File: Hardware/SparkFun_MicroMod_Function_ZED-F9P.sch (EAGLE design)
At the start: 107 parts, among them J10 QWIIC_RA, J11 Bus Selection, J12 USB Female Type C Connector, J2 MICROMOD_STANDARD, J3 QWIIC_RA, J4 U.FL, J5 455-1750-1-ND, J8 Bus Selection, Q1 DMP21D0UT, U1 EEPROM, U10 OPA344, U11 74LVC4066D_QUAD_BILATERAL_SWI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, U12 74LVC4066D_QUAD_BILATERAL_SWI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, U2 U-BLOX_ZED-F9P, U3 FIN1017MXSOIC-8, U4 SN74AUP1T04DCK, U5 SN74LVC1G66DRYR, U6 74LVC541ABQ, U7 3.3V, U9 SN74AUP1T04DCK

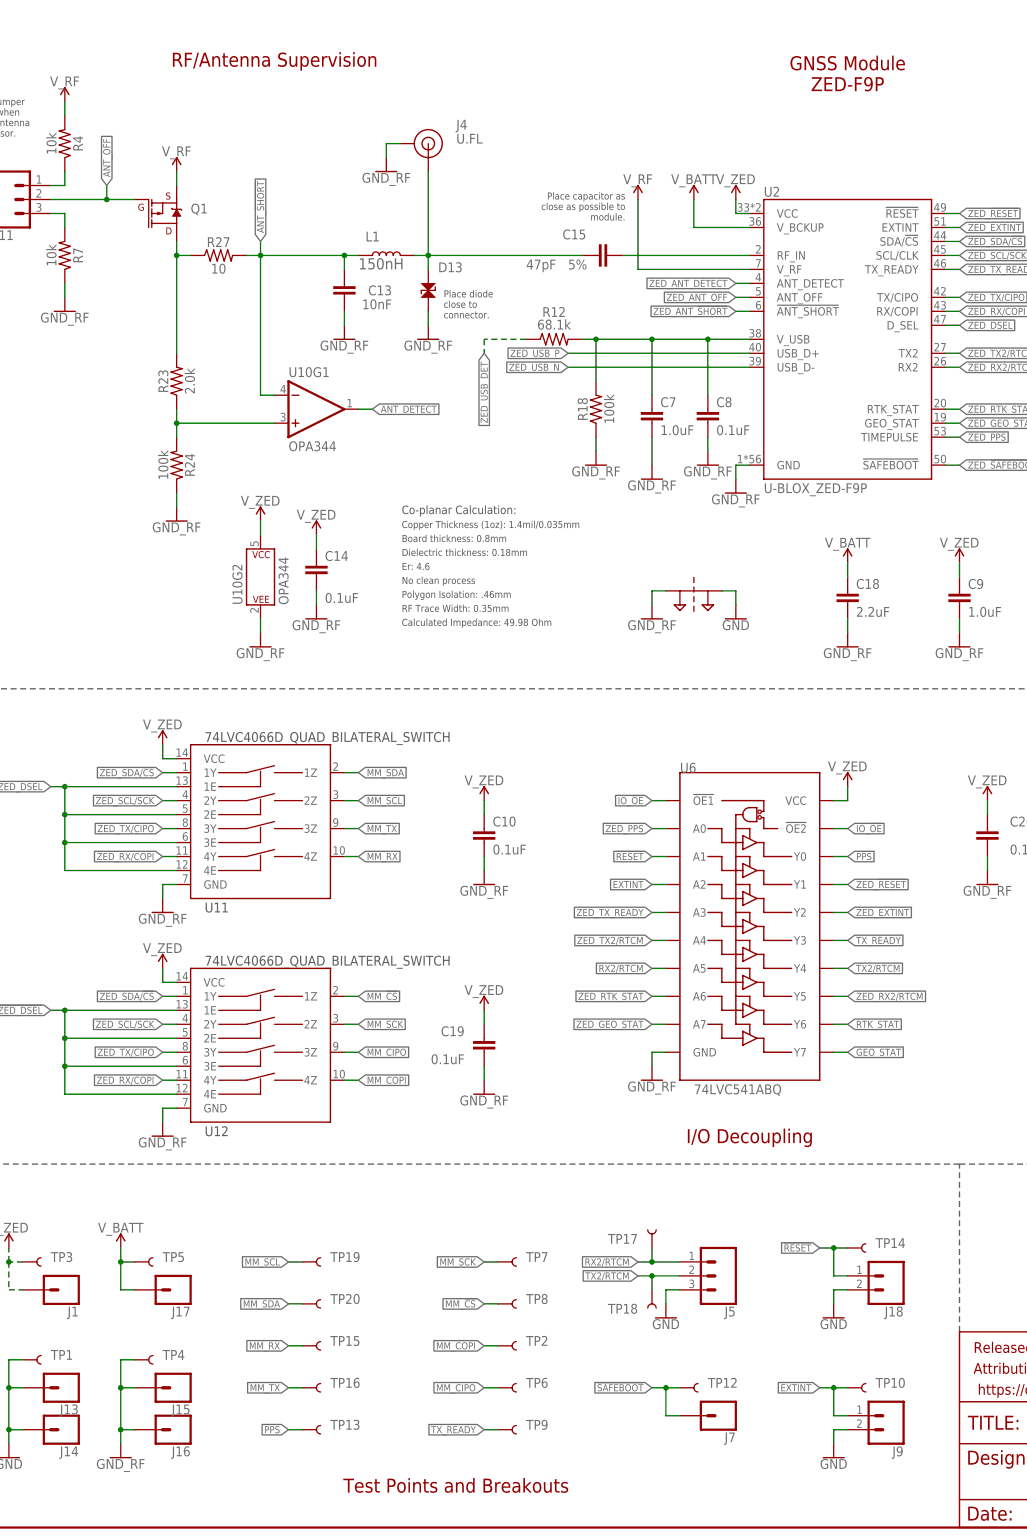
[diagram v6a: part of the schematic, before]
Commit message: ERC run and fixes applied.
Forgot to do that before previous commit.
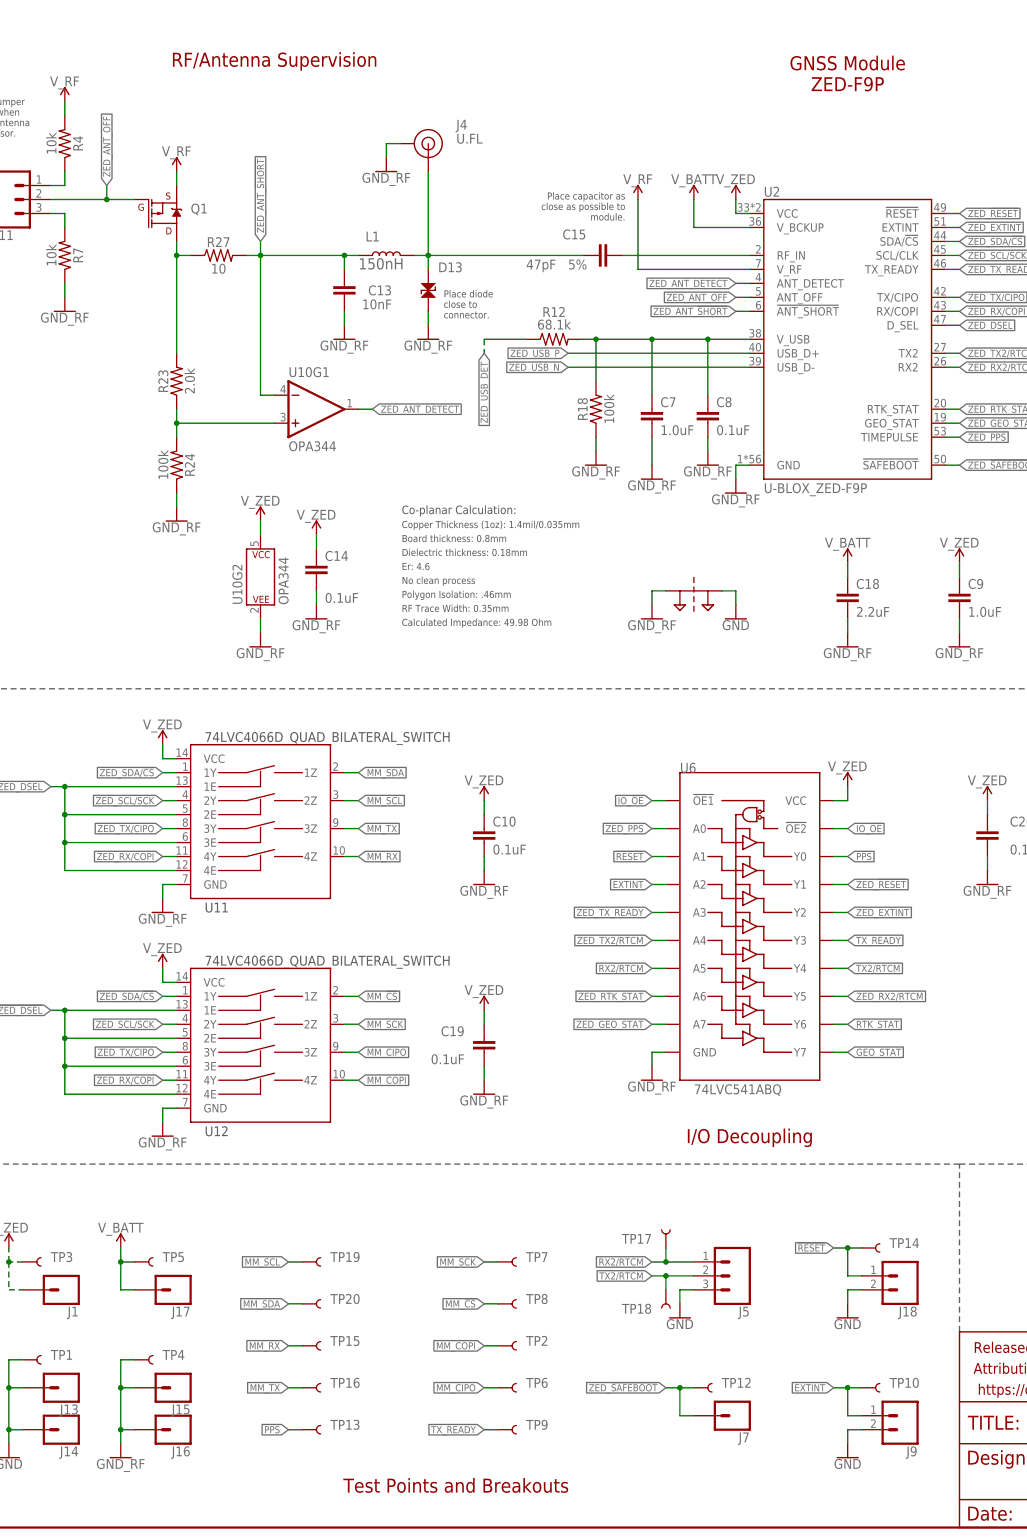
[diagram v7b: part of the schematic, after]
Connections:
- removed net !SAFEBOOT!: J7.1, TP12.1
- removed net ANT_!SHORT!: C13.1, L1.1, R27.2, U10G1.-IN
- removed net ANT_DETECT: U10G1.OUT
- removed net ANT_OFF: J11.2, Q1.G
- new net N$14: C7.1, C8.1, R12.2, R18.2, U2.V_USB
- net ZED_!SAFEBOOT!: now also J7.1, TP12.1
- net ZED_ANT_!SHORT!: now also C13.1, L1.1, R27.2, U10G1.-IN
- net ZED_ANT_DETECT: now also U10G1.OUT
- net ZED_ANT_OFF: now also J11.2, Q1.G
- net ZED_USB_DET: no longer C7.1, C8.1, R12.2, R18.2, U2.V_USB
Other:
- moved on the sheet: J18, J5, J7, J9, TP10, TP12, TP14, TP17, TP18

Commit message: First day of layout.
Laid out most of the board with airwires. Have a rough idea of grounding so far so good. Have had to replace a fair bit of components for smaller ones. Those 0603's look massive on such a small board.
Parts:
- removed C17, C19, C20: 0.1uF, SparkFun-Capacitors:0.1UF-0603-25V-(+80/-20%)
- removed C18: 2.2uF, SparkFun-Capacitors:2.2UF-0402_TIGHT-10V-10%-X5R
- removed D13: PESD0402, SparkFun-DiscreteSemi:PESD0402
- removed D9: 3A/10V/280mV, SparkFun-DiscreteSemi:DIODE-SCHOTTKY-BAT60A
- removed JP9: JUMPER-SMT_2_NC_TRACE_SILK, SparkFun-Jumpers:JUMPER-SMT_2_NC_TRACE_SILK
- removed R20: 1k, SparkFun-Resistors:1KOHM-0603-1/10W-1%
- removed R23: 2.0k, SparkFun-Resistors:2.0KOHM-0603-1/10W-5%
- removed TP20: TEST-POINT3, SparkFun-Connectors:TEST-POINT3
- removed U12: 74LVC4066D_QUAD_BILATERAL_SWITCH, SparkFun-IC-Logic:74LVC4066D_QUAD_BILATERAL_SWITCH
- added C16, C4, C6: 0.1uF, SparkFun-Capacitors:0.1UF-0402T-16V-10%
- added C5: 10nF, SparkFun-Capacitors:10NF-0402T-25V-10%-X7R-WE
- added D2: 3A/10V/280mV, SparkFun-DiscreteSemi:DIODE-SCHOTTKY-BAT60A
- added D8: PESD0402-0402T, SparkFun-DiscreteSemi:PESD0402-0402T
- added JP6: JUMPER-SMT_2_NC_TRACE_SILK, SparkFun-Jumpers:JUMPER-SMT_2_NC_TRACE_SILK
- added R15: 68.1k, SparkFun-Resistors:68.1KOHM-0603-1/10W-1%
- added R17: 10k, SparkFun-Resistors:10KOHM-0603-1/10W-1%
- added TP11: TEST-POINT3, SparkFun-Connectors:TEST-POINT3
- added U8: U-BLOX_ZED-F9P, MicroMod_Function_GNSS_ublox_ZED_F9P:U-BLOX_ZED-F9P
- C1, C3, C9: device SparkFun-Capacitors:1.0UF-0603-16V-10% -> SparkFun-Capacitors:1.0UF-0402T-16V-10%
- C10, C14: device SparkFun-Capacitors:0.1UF-0402-16V-10% -> SparkFun-Capacitors:0.1UF-0402T-16V-10%
- C11: value 0.1uF -> 2.2uF; device SparkFun-Capacitors:0.1UF-0603-25V-(+80/-20%) -> SparkFun-Capacitors:2.2UF-0402_TIGHT-10V-10%-X5R
- C12: value 0.1uF -> 1.0uF; device SparkFun-Capacitors:0.1UF-0402-16V-10% -> SparkFun-Capacitors:1.0UF-0402T-16V-10%
- C13: value 10nF -> 0.1uF; device SparkFun-Capacitors:10NF-0402T-25V-10%-X7R-WE -> SparkFun-Capacitors:0.1UF-0402T-16V-10%
- C15: value CBR04C470J5GAC -> 0.1uF; device MicroMod_Function_GNSS_ublox_ZED_F9P:CBR04C470J5GAC -> SparkFun-Capacitors:0.1UF-0402T-16V-10%
- C2: device SparkFun-Capacitors:0.1UF-0603-25V-(+80/-20%) -> SparkFun-Capacitors:0.1UF-0402T-16V-10%
- C7: value 1.0uF -> 0.1uF; device SparkFun-Capacitors:1.0UF-0603-16V-10% -> SparkFun-Capacitors:0.1UF-0402T-16V-10%
- C8: value 0.1uF -> CBR04C470J5GAC; device SparkFun-Capacitors:0.1UF-0402T-16V-10% -> MicroMod_Function_GNSS_ublox_ZED_F9P:CBR04C470J5GAC
- D3: value BLUE -> PRTR5V0U2F; device SparkFun-LED:LED-BLUE0603 -> SparkFun-IC-Power:PRTR5V0U2F
- D4: value BLUE -> 0.5A/40V/420mV; device SparkFun-LED:LED-BLUE0603 -> SparkFun-DiscreteSemi:DIODE-SCHOTTKY-PMEG4005EJ
- D6: value PRTR5V0U2F -> BLUE; device SparkFun-IC-Power:PRTR5V0U2F -> SparkFun-LED:LED-BLUE0603
- D7: value 0.5A/40V/420mV -> BLUE; device SparkFun-DiscreteSemi:DIODE-SCHOTTKY-PMEG4005EJ -> SparkFun-LED:LED-BLUE0603
- J1: value (none) -> USB Female Type C Connector; device SparkFun-Connectors:CONN_01 -> SparkFun-Connectors:USB_C_4-LAYER-ISOLATED
- J10: value QWIIC_RA -> U.FL; device SparkFun-Connectors:QWIIC_CONNECTORJS-1MM -> SparkFun-Connectors:U.FL2PIN
- J11: value Bus Selection -> 455-1750-1-ND; device SparkFun-Connectors:CONN_03LOCK -> SparkFun-Connectors:CONN_03
- J12: value USB Female Type C Connector -> (none); device SparkFun-Connectors:USB_C_4-LAYER-ISOLATED -> SparkFun-Connectors:CONN_01
- J13, J14: device SparkFun-Connectors:CONN_01 -> SparkFun-Connectors:CONN_02
- J15, J16: value (none) -> QWIIC_RA; device SparkFun-Connectors:CONN_01 -> SparkFun-Connectors:QWIIC_CONNECTORJS-1MM
- J17: device SparkFun-Connectors:CONN_01 -> SparkFun-Connectors:CONN_04PTH
- J18: value (none) -> Bus Selection; device SparkFun-Connectors:CONN_02 -> SparkFun-Connectors:CONN_03LOCK
- J3: value QWIIC_RA -> Bus Selection; device SparkFun-Connectors:QWIIC_CONNECTORJS-1MM -> SparkFun-Connectors:CONN_03LOCK
- J4: value U.FL -> (none); device SparkFun-Connectors:U.FL2PIN -> SparkFun-Connectors:CONN_01
- J5: value 455-1750-1-ND -> (none); device SparkFun-Connectors:CONN_03 -> SparkFun-Connectors:CONN_01
- J6: device SparkFun-Connectors:CONN_04PTH -> SparkFun-Connectors:CONN_01
- J8: value Bus Selection -> (none); device SparkFun-Connectors:CONN_03LOCK -> SparkFun-Connectors:CONN_01
- J9: device SparkFun-Connectors:CONN_02 -> SparkFun-Connectors:CONN_01
- R10: value 27 -> 10k; device SparkFun-Resistors:27OHM -> SparkFun-Resistors:10KOHM-0603-1/10W-1%
- R11: value 3.3k -> 10k; device SparkFun-Resistors:3.3KOHM-0603-1/10W-1% -> SparkFun-Resistors:10KOHM-0603-1/10W-1%
- R12: value 68.1k -> 1k; device SparkFun-Resistors:68.1KOHM-0603-1/10W-1% -> SparkFun-Resistors:1KOHM-0603-1/10W-1%; RESISTANCE (none) -> 1k
- R3: value 10k -> 5.1k; device SparkFun-Resistors:10KOHM-0603-1/10W-1% -> SparkFun-Resistors:5.1KOHM5.1KOHM-0603-1/10W-1%
- R4: value 10k -> 3.3k; device SparkFun-Resistors:10KOHM-0603-1/10W-1% -> SparkFun-Resistors:3.3KOHM-0603-1/10W-1%
- R5, R6: value 1k -> 27; device SparkFun-Resistors:1KOHM-0603-1/10W-1% -> SparkFun-Resistors:27OHM
- R7: value 10k -> 1k; device SparkFun-Resistors:10KOHM-0603-1/10W-1% -> SparkFun-Resistors:1KOHM-0603-1/10W-1%
- R8: value 5.1k -> 1k; device SparkFun-Resistors:5.1KOHM5.1KOHM-0603-1/10W-1% -> SparkFun-Resistors:1KOHM-0603-1/10W-1%
- R9: value 27 -> 1k; device SparkFun-Resistors:27OHM -> SparkFun-Resistors:1KOHM-0603-1/10W-1%
- U1: value EEPROM -> SN74LVC1G66DRYR; device SparkFun-IC-Memory:EEPROM-I2C512K -> MicroMod_Function_GNSS_ublox_ZED_F9P:SN74LVC1G66DRYR
- U10: value OPA344 -> SN74AUP1T04DCK; device SparkFun-IC-Amplifiers:OPA344 -> MicroMod_Function_GNSS_ublox_ZED_F9P:SN74AUP1T04DCK
- U11: value 74LVC4066D_QUAD_BILATERAL_SWITCH -> SN74AUP1T04DCK; device SparkFun-IC-Logic:74LVC4066D_QUAD_BILATERAL_SWITCH -> MicroMod_Function_GNSS_ublox_ZED_F9P:SN74AUP1T04DCK
- U2: value U-BLOX_ZED-F9P -> 3.3V; device MicroMod_Function_GNSS_ublox_ZED_F9P:U-BLOX_ZED-F9P -> SparkFun-IC-Power:V_REG_AP2112K-3.3V
- U3: value FIN1017MXSOIC-8 -> EEPROM; device MicroMod_Function_GNSS_ublox_ZED_F9P:FIN1017MXSOIC-8 -> SparkFun-IC-Memory:EEPROM-I2C512K
- U4: value SN74AUP1T04DCK -> 74LVC4066D_QUAD_BILATERAL_SWITCH; device MicroMod_Function_GNSS_ublox_ZED_F9P:SN74AUP1T04DCK -> SparkFun-IC-Logic:74LVC4066D_QUAD_BILATERAL_SWITCH
- U5: value SN74LVC1G66DRYR -> 74LVC4066D_QUAD_BILATERAL_SWITCH; device MicroMod_Function_GNSS_ublox_ZED_F9P:SN74LVC1G66DRYR -> SparkFun-IC-Logic:74LVC4066D_QUAD_BILATERAL_SWITCH
- U6: value 74LVC541ABQ -> OPA344; device MicroMod_Function_GNSS_ublox_ZED_F9P:74LVC541ABQ -> SparkFun-IC-Amplifiers:OPA344
- U7: value 3.3V -> 74LVC541ABQ; device SparkFun-IC-Power:V_REG_AP2112K-3.3V -> MicroMod_Function_GNSS_ublox_ZED_F9P:74LVC541ABQ
- U9: value SN74AUP1T04DCK -> FIN1017MXSOIC-8; device MicroMod_Function_GNSS_ublox_ZED_F9P:SN74AUP1T04DCK -> MicroMod_Function_GNSS_ublox_ZED_F9P:FIN1017MXSOIC-8
- renumbered D11 to D5, JP13 to JP3, R18 to R16, R24 to R13, R27 to R14, SUPPLY35 to SUPPLYTIE1
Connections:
- removed net VDD: C1.1, J1.1, R3.2, TP3.1, U7.OUT
- net !RESET!: now also J13.1, TP18.1, U7.A1; no longer J18.1, TP14.1, U6.A1
- net !ZED_DSEL!: now also U11.Y, U5.1E, U5.2E, U5.3E, U5.4E; no longer U12.1E, U12.2E, U12.3E, U12.4E, U9.Y
- net 3.3V: now also C14.1, D4.A, J15.2, J16.2, U9.VCC; no longer C12.1, D7.A, J10.2, J3.2, U1.VCC
- net 5V: now also C1.1, D2.C, U2.IN; no longer C3.1, D9.C, U5.CTRL_IN, U5.VCC, U7.IN
- net A0: now also U3.A0; no longer U1.A0
- net A1: now also U3.A1; no longer U1.A1
- net A2: now also U3.A2; no longer U1.A2
- net EWP: now also JP2.2, U3.WP; no longer JP1.2, U1.WP
- net EXTINT: now also J14.1, TP19.1, U7.A2; no longer J9.1, TP10.1, U6.A2
- net GEO_STAT: now also U7.Y7; no longer U6.Y7
- net GND: now also C14.2, D3.2, J1.GND, J11.3, J13.2, J14.2, J15.1, J16.1, J17.1, J17.4, J5.1, JP2.1, JP4.2, JP6.1, R3.1, TP2.1, U1.VSS, U2.GND, U9.GND; no longer C12.2, D6.2, J10.1, J12.GND, J13.1, J14.1, J18.2, J3.1, J5.3, J6.4, J9.2, JP1.1, JP4.1, JP9.2, R8.1, TP1.1, U1.GND, U5.VSS, U7.GND
- net GND_RF: now also C11.2, C12.2, C15.2, C16.2, C4.2, C5.2, C6.2, D8.2, J10.GND, J18.3, J8.1, J9.1, R11.1, U10.GND, U5.GND, U6G2.P$V-, U7.GND, U8.GND; no longer C11.1, C14.1, C17.1, C18.2, C19.2, C20.2, C8.2, D13.2, J15.1, J16.1, J4.GND, J8.3, R7.1, U10G2.P$V-, U12.GND, U2.GND, U6.GND, U9.GND
- net IO_!OE!: now also U10.Y, U7.!OE1!, U7.!OE2!; no longer U4.Y, U6.!OE1!, U6.!OE2!
- net MM_!CS!: now also TP11.1, U5.1Z; no longer TP8.1, U12.1Z
- net MM_CIPO: now also TP13.1, U5.3Z; no longer TP6.1, U12.3Z
- net MM_COPI: now also TP12.1, U5.4Z; no longer TP2.1, U12.4Z
- net MM_RX: now also TP7.1, U4.4Z; no longer TP15.1, U11.4Z
- net MM_SCK: now also TP10.1, U5.2Z; no longer TP7.1, U12.2Z
- net MM_SCL: now also J15.4, J16.4, TP5.1, U3.SCL, U4.2Z; no longer J10.4, J3.4, TP19.1, U1.SCL, U11.2Z
- net MM_SDA: now also J15.3, J16.3, TP6.1, U3.SDA, U4.1Z; no longer J10.3, J3.3, TP20.1, U1.SDA, U11.1Z
- net MM_TX: now also TP8.1, U4.3Z; no longer TP16.1, U11.3Z
- net N$1: now also D3.3, J1.D+; no longer D6.1, J12.D+
- net N$10: now also J18.1, R17.1; no longer J8.1, R3.1
- net N$11: now also J3.1, R10.1; no longer J11.1, R4.1
- net N$12: now also J3.3, R11.2; no longer J11.3, R7.2
- net N$13: now also R12.1; no longer R23.2
- net N$14: now also C10.1, C9.1, R15.2, U8.V_USB; no longer C7.1, C8.1, R12.2, U2.V_USB
- net N$16: now also D2.A, JP1.2; no longer D1.A, JP2.2
- net N$2: now also D3.1, J1.D-; no longer D6.3, J12.D-
- net N$26: now also JP4.1, R7.1; no longer JP9.1, R20.1
- net N$27: now also JP5.2, R8.1; no longer JP4.2, R5.1
- net N$28: now also D6.C, R8.2; no longer D3.C, R5.2
- net N$29: now also D7.C, R9.2; no longer D4.C, R6.2
- net N$3: now also J1.CC2; no longer J12.CC2
- net N$30: now also R7.2; no longer R20.2
- net N$32: now also D4.C, R4.2; no longer D7.C, R11.2
- net N$4: now also J1.CC1, R3.2; no longer J12.CC1, R8.2
- net N$48: now also R12.2, U6G1.+IN; no longer R23.1, U10G1.+IN
- net N$5: now also D3.4, R5.1; no longer D6.6, R9.1
- net N$51: now also J17.3, U9.DO-; no longer J6.3, U3.DO-
- net N$6: now also D3.6, R6.1; no longer D6.4, R10.1
- net N$7: now also C8.1, D8.1, J10.SIGNAL; no longer C15.1, D13.1, J4.SIGNAL
- net N$8: now also JP6.2, R9.1; no longer JP5.2, R6.1
- net N$9: now also J17.2, U9.DO+; no longer J6.2, U3.DO+
- net PPS: now also D6.A, TP9.1, U7.Y0, U9.DIN; no longer D3.A, TP13.1, U3.DIN, U6.Y0
- net PWR_EN: now also U2.EN; no longer U7.EN
- net RF_IN: now also C8.2, U8.RF_IN; no longer C15.2, U2.RF_IN
- net RTK_STAT: now also D7.A, U7.Y6; no longer D4.A, U6.Y6
- net RX2/RTCM: now also J11.1, TP15.1, U7.A5; no longer J5.1, TP17.1, U6.A5
- net SHLD: now also J1.SHLD; no longer J12.SHLD
- net TX2/RTCM: now also J11.2, TP16.1, U7.Y4; no longer J5.2, TP18.1, U6.Y4
- net TX_READY: now also TP14.1, U7.Y3; no longer TP9.1, U6.Y3
- net VIN: now also D1.A; no longer D9.A
- net V_BATT: now also C11.1, J7.1, R4.1, TP3.1, U8.V_BCKUP; no longer C18.1, J17.1, R11.1, TP5.1, U2.V_BCKUP
- net V_RF: now also R10.2, U8.V_RF; no longer R4.2, U2.V_RF
- net V_USB: now also D3.5, J1.VBUS, JP1.1, U1.A_IN; no longer D6.5, J12.VBUS, JP2.1, U5.A_IN
- net V_ZED: now also C12.1, C13.1, C15.1, C16.1, C3.1, C4.1, C6.1, C7.1, J4.1, R17.2, TP1.1, U1.CTRL_IN, U1.VCC, U10.A, U10.VCC, U2.OUT, U5.VCC, U6G2.P$V+, U7.VCC, U8.VCC; no longer C10.1, C11.2, C14.2, C17.2, C19.1, C20.1, C9.1, U10G2.P$V+, U12.VCC, U2.VCC, U4.A, U6.VCC, U9.VCC
- net ZED_!RESET!: now also U7.Y1, U8.!RESET!; no longer U2.!RESET!, U6.Y1
- net ZED_!SAFEBOOT!: now also J12.1, TP17.1, U8.!SAFEBOOT!; no longer J7.1, TP12.1, U2.!SAFEBOOT!
- net ZED_ANT_!SHORT!: now also C5.1, U6G1.-IN, U8.!ANT_SHORT!; no longer C13.1, U10G1.-IN, U2.!ANT_SHORT!
- net ZED_ANT_DETECT: now also U6G1.OUT, U8.ANT_DETECT; no longer U10G1.OUT, U2.ANT_DETECT
- net ZED_ANT_OFF: now also J3.2, U8.ANT_OFF; no longer J11.2, U2.ANT_OFF
- net ZED_DSEL: now also J18.2, U11.A, U4.1E, U4.2E, U4.3E, U4.4E, U8.D_SEL; no longer J8.2, U11.1E, U11.2E, U11.3E, U11.4E, U2.D_SEL, U9.A
- net ZED_EXTINT: now also U7.Y2, U8.EXTINT; no longer U2.EXTINT, U6.Y2
- net ZED_GEO_STAT: now also U7.A7, U8.GEO_STAT; no longer U2.GEO_STAT, U6.A7
- net ZED_PPS: now also U7.A0, U8.TIMEPULSE; no longer U2.TIMEPULSE, U6.A0
- net ZED_RTK_STAT: now also U7.A6, U8.RTK_STAT; no longer U2.RTK_STAT, U6.A6
- net ZED_RX/COPI: now also U4.4Y, U5.4Y, U8.RX/COPI; no longer U11.4Y, U12.4Y, U2.RX/COPI
- net ZED_RX2/RTCM: now also U7.Y5, U8.RX2; no longer U2.RX2, U6.Y5
- net ZED_SCL/SCK: now also U4.2Y, U5.2Y, U8.SCL/CLK; no longer U11.2Y, U12.2Y, U2.SCL/CLK
- net ZED_SDA/!CS!: now also U4.1Y, U5.1Y, U8.SDA/!CS!; no longer U11.1Y, U12.1Y, U2.SDA/!CS!
- net ZED_TX/CIPO: now also U4.3Y, U5.3Y, U8.TX/CIPO; no longer U11.3Y, U12.3Y, U2.TX/CIPO
- net ZED_TX2/RTCM: now also U7.A4, U8.TX2; no longer U2.TX2, U6.A4
- net ZED_TX_READY: now also U7.A3, U8.TX_READY; no longer U2.TX_READY, U6.A3
- net ZED_USB_DET: now also R15.1, U1.A_OUT; no longer R12.1, U5.A_OUT
- net ZED_USB_N: now also R6.2, U8.USB_D-; no longer R10.2, U2.USB_D-
- net ZED_USB_P: now also R5.2, U8.USB_D+; no longer R9.2, U2.USB_D+
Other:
- moved on the sheet: C1, C10, C11, C12, C13, C14, C15, C3, C7, C8, C9, D1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
